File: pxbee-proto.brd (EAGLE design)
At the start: 58.4 x 67.3 mm, 2 parts

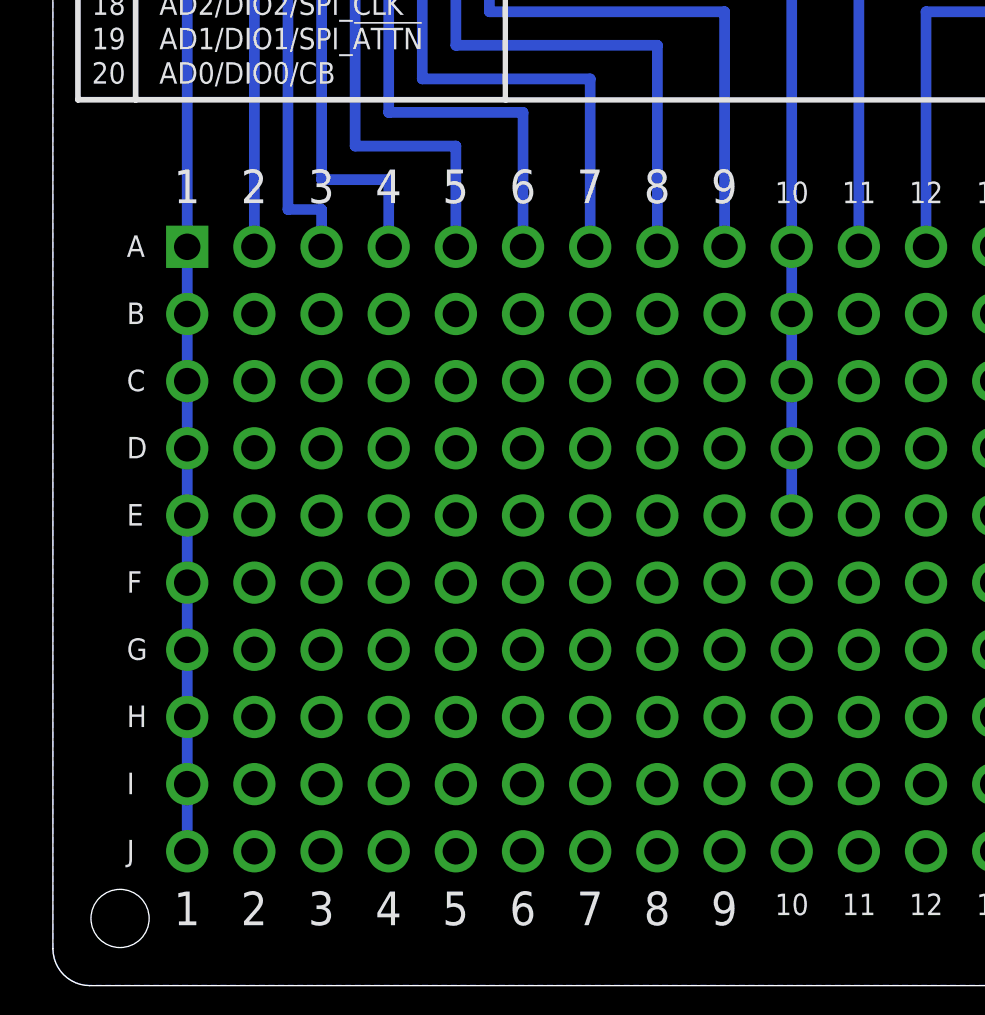
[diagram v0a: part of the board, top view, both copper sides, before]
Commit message: Update prototype component; Mark VCC and GND area
- VCC and GND area are now marked in silkscreen layer
- Addresses findings in #1
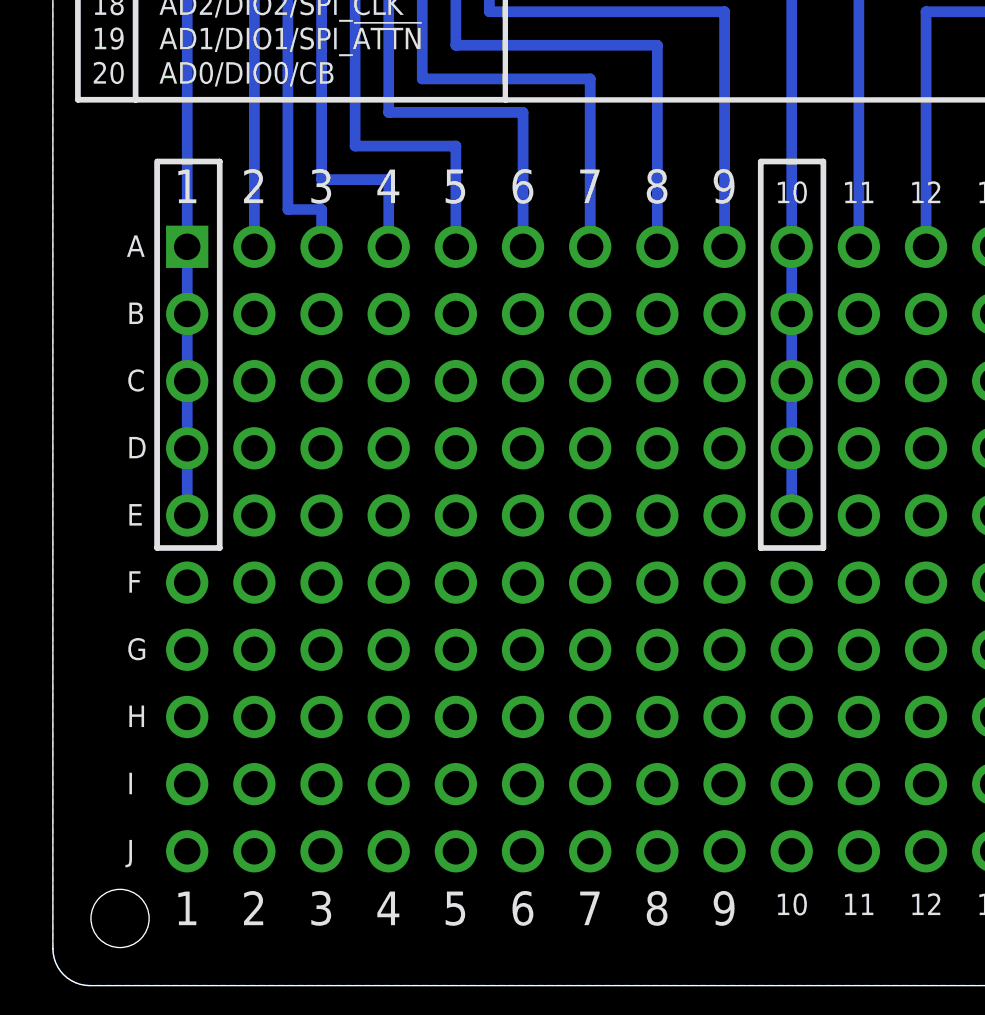
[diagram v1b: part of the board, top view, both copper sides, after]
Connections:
- net N$1: no longer U$2.P1-F, U$2.P1-G, U$2.P1-H, U$2.P1-I, U$2.P1-J
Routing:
- net N$1: track 67.6 -> 54.9 mm
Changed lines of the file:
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@@
 <wire x1="0.94731875" y1="62.497640625" x2="0.94731875" y2="36.040390625" width="0.2159" layer="21"/>
 <wire x1="3.129534375" y1="36.040390625" x2="3.129534375" y2="62.497640625" width="0.2159" layer="21"/>
+<wire x1="3.941521875" y1="33.705928125" x2="3.941521875" y2="19.09015625" width="0.2159" layer="21"/>
+<wire x1="3.941521875" y1="19.09015625" x2="6.30981875" y2="19.09015625" width="0.2159" layer="21"/>
+<wire x1="6.30981875" y1="19.09015625" x2="6.30981875" y2="33.705928125" width="0.2159" layer="21"/>
+<wire x1="6.30981875" y1="33.705928125" x2="3.966896875" y2="33.705928125" width="0.2159" layer="21"/>
+<wire x1="26.770203125" y1="33.705928125" x2="26.770203125" y2="19.09015625" width="0.2159" layer="21"/>
+<wire x1="26.770203125" y1="19.09015625" x2="29.1385" y2="19.09015625" width="0.2159" layer="21"/>
+<wire x1="29.1385" y1="19.09015625" x2="29.1385" y2="33.705928125" width="0.2159" layer="21"/>
+<wire x1="29.1385" y1="33.705928125" x2="26.795578125" y2="33.705928125" width="0.2159" layer="21"/>
 </plain>
 <attributes>
@@
 <contactref element="U$2" pad="P1-D"/>
 <contactref element="U$2" pad="P1-E"/>
-<contactref element="U$2" pad="P1-F"/>
-<contactref element="U$2" pad="P1-G"/>
-<contactref element="U$2" pad="P1-H"/>
-<contactref element="U$2" pad="P1-I"/>
-<contactref element="U$2" pad="P1-J"/>
 <wire x1="5.08" y1="30.48" x2="5.08" y2="62.08674375" width="0.4064" layer="16"/>
 <wire x1="5.118459375" y1="62.086" x2="5.08" y2="62.08674375" width="0.4064" layer="16"/>
@@
 <wire x1="5.08" y1="25.4" x2="5.08" y2="22.86" width="0.4064" layer="16"/>
 <wire x1="5.08" y1="22.86" x2="5.08" y2="20.32" width="0.4064" layer="16"/>
-<wire x1="5.08" y1="20.32" x2="5.08" y2="17.78" width="0.4064" layer="16"/>
-<wire x1="5.08" y1="17.78" x2="5.08" y2="15.24" width="0.4064" layer="16"/>
-<wire x1="5.08" y1="15.24" x2="5.08" y2="12.7" width="0.4064" layer="16"/>
-<wire x1="5.08" y1="12.7" x2="5.08" y2="10.16" width="0.4064" layer="16"/>
-<wire x1="5.08" y1="10.16" x2="5.08" y2="7.62" width="0.4064" layer="16"/>
 </signal>
 <signal name="N$2">
